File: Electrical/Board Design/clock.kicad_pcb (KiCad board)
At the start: 2 copper layers, 31 parts, among them CON1 AVR-ISP-6, IC1 ATTINY84A-SS, Q1 FET_N, Q2 FET_P, SW1 SPST, U1 MCP1624

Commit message: big catchup
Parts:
- added BT1: BATTERY, AA_battery_clip, F.Cu at (258.2, 216.9)
- added BT2: BATTERY, AA_battery_clip, F.Cu at (192.3, 216.9)
- added D1: DIODE, SIL-2, F.Cu at (200.8, 184.9)
- added D2: LED, SIL-2, F.Cu at (176.3, 181.9)
- added D3: LED, SIL-2, F.Cu at (226.7, 181.5)
- added SP1: SPEAKER, SIL-2, F.Cu at (200.8, 181.3)
- added X1: CRYSTAL 32.768kHz, CRYSTAL, F.Cu at (198.7, 201.6)
- S1: footprint bourns_encoder -> bourns_knob
- moved S1 227.0 mm to (249.3, 182.2)
- moved R12 220.7 mm to (252.3, 195.7)
- moved C6 220.7 mm to (256.1, 198.2)
- moved R11 220.7 mm to (256.1, 193.2)
- moved R9 219.5 mm to (248.0, 194.5)
- moved R10 217.2 mm to (243.2, 189.6)
- moved C5 216.3 mm to (243.2, 193.4)
- moved R3 171.2 mm to (142.6, 188.6), turned to 270 degrees
- moved R2 168.9 mm to (150.3, 182.2)
- moved Q1 168.9 mm to (146.2, 194.7)
- moved R1 168.9 mm to (146.2, 189.6)
- moved R4 167.1 mm to (149.9, 197.9)
- moved Q2 167.1 mm to (139.0, 188.5)
- moved SW1 165.4 mm to (136.9, 196.3)
- moved R15 158.4 mm to (225.4, 185.6)
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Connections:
- R12 pad 2: /INT 2 -> /INT 1
- R9 pad 1: /INT 1 -> /INT 2
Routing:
- net N-000002: track 0.00 -> 128.5 mm, vias 0 -> 4
- net VCC: track 0.00 -> 101.4 mm, vias 0 -> 5
- net GND: track 0.00 -> 67.4 mm, vias 0 -> 10
- net N-000004: track 0.00 -> 67.3 mm
- net /MODE SELECT POWER: track 0.00 -> 63.2 mm
- net /ALARM LIGHT: track 0.00 -> 57.7 mm, vias 0 -> 2
- net /INT 1: track 0.00 -> 56.6 mm
- net /MODE SELECT: track 0.00 -> 53.9 mm
- net /INT 2: track 0.00 -> 53.8 mm
- net /AM PM LIGHT: track 0.00 -> 47.4 mm, vias 0 -> 2
- net /ALARM BUZZER: track 0.00 -> 28.2 mm, vias 0 -> 3
- net N-000009: track 0.00 -> 26.5 mm, vias 0 -> 2
- net N-0000018: track 0.00 -> 20.8 mm
- net N-0000015: track 0.00 -> 18.6 mm
- net N-0000022: track 0.00 -> 17.2 mm
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- added copper zone on B.Cu, net GND
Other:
- board outline added: 133.3 x 44.5 mm
- board text removed: "AMMETERS"

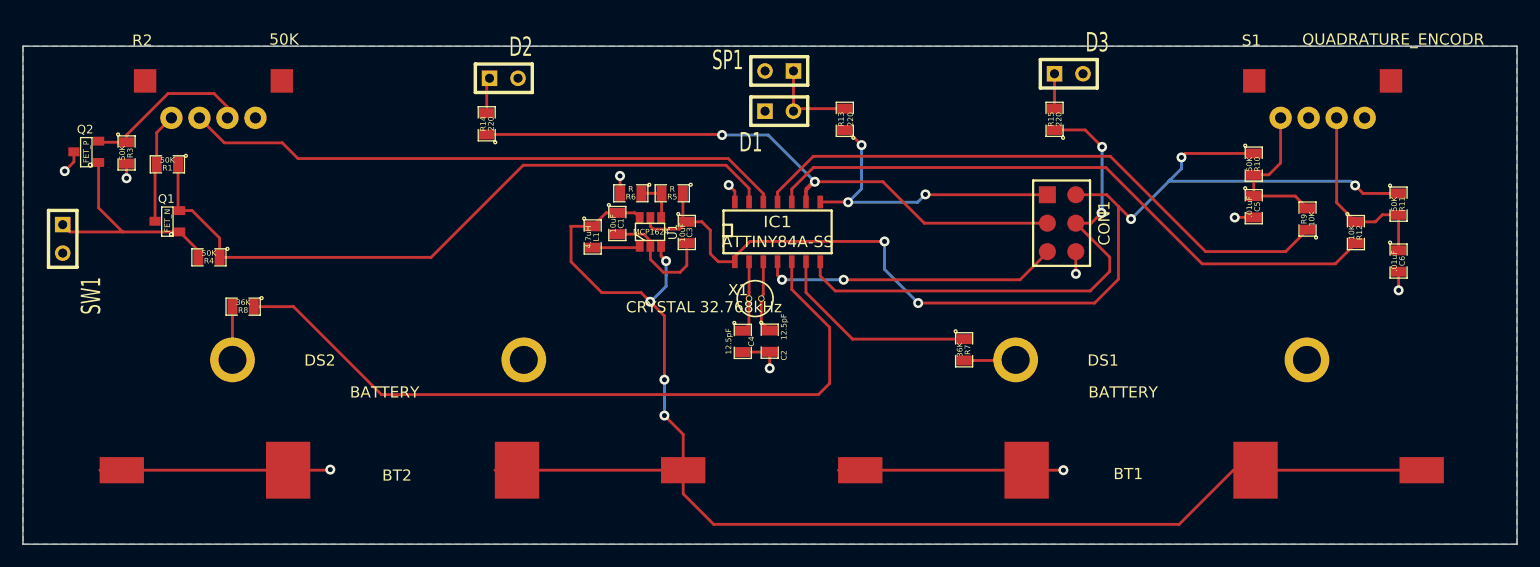
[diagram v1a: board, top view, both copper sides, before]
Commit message: board layout updates for battery stuff
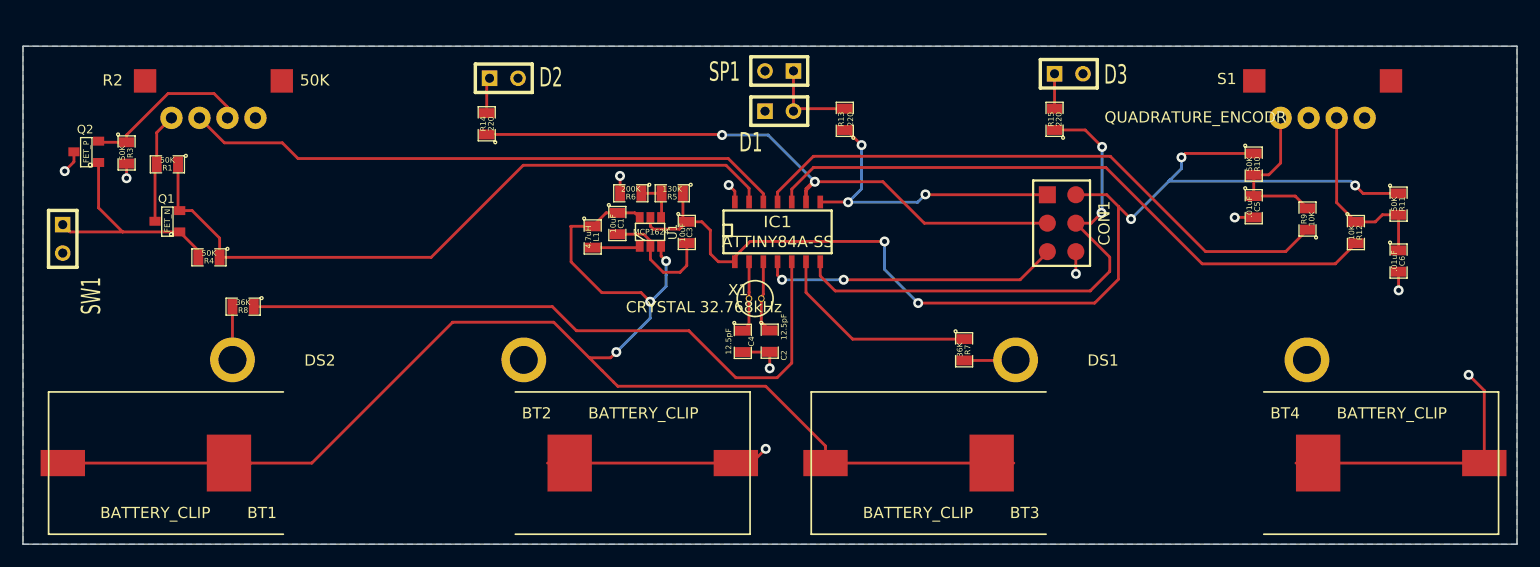
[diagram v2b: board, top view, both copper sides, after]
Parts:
- added BT3: BATTERY_CLIP, AA_battery_clip_single, F.Cu at (213.2, 216.3)
- added BT4: BATTERY_CLIP, AA_battery_clip_single, F.Cu at (255.5, 216.3)
- BT1, BT2: value BATTERY -> BATTERY_CLIP; footprint AA_battery_clip -> AA_battery_clip_single
- R5: value R -> 130K
- R6: value R -> 200K
- moved BT1 113.0 mm to (145.2, 216.3), turned to 270 degrees
- moved BT2 3.61 mm to (188.7, 216.3)
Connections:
- C1 pad 1: N-000002 (its old number) -> N-000006
- L1 pad 1: N-000002 (its old number) -> N-000006
- U1 pad 3: N-000002 (its old number) -> N-000006
- U1 pad 6: N-000002 (its old number) -> N-000006
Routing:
- net N-000006: track 0.00 -> 128.9 mm, vias 0 -> 3
- net N-000002 (its old number): track 128.5 -> 0.00 mm, vias 4 -> 0
- net N-000004: track 67.3 -> 60.2 mm
- net GND: track 67.4 -> 72.0 mm

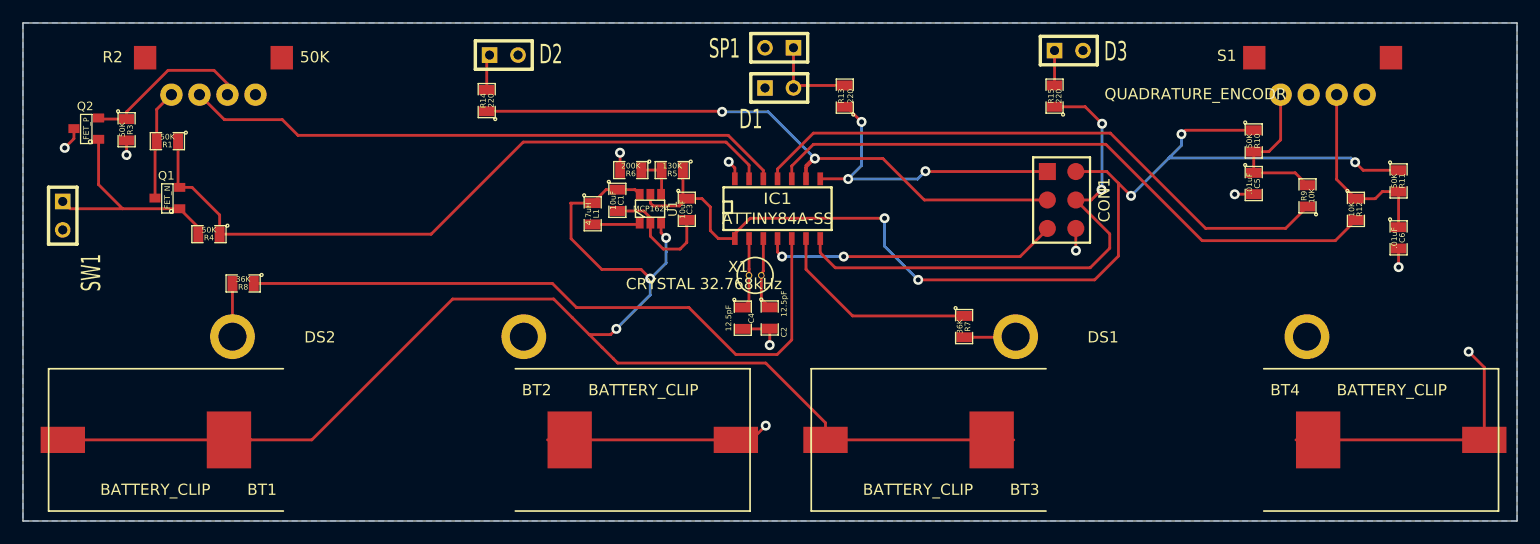
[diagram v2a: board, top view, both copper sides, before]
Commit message: updates to board layout
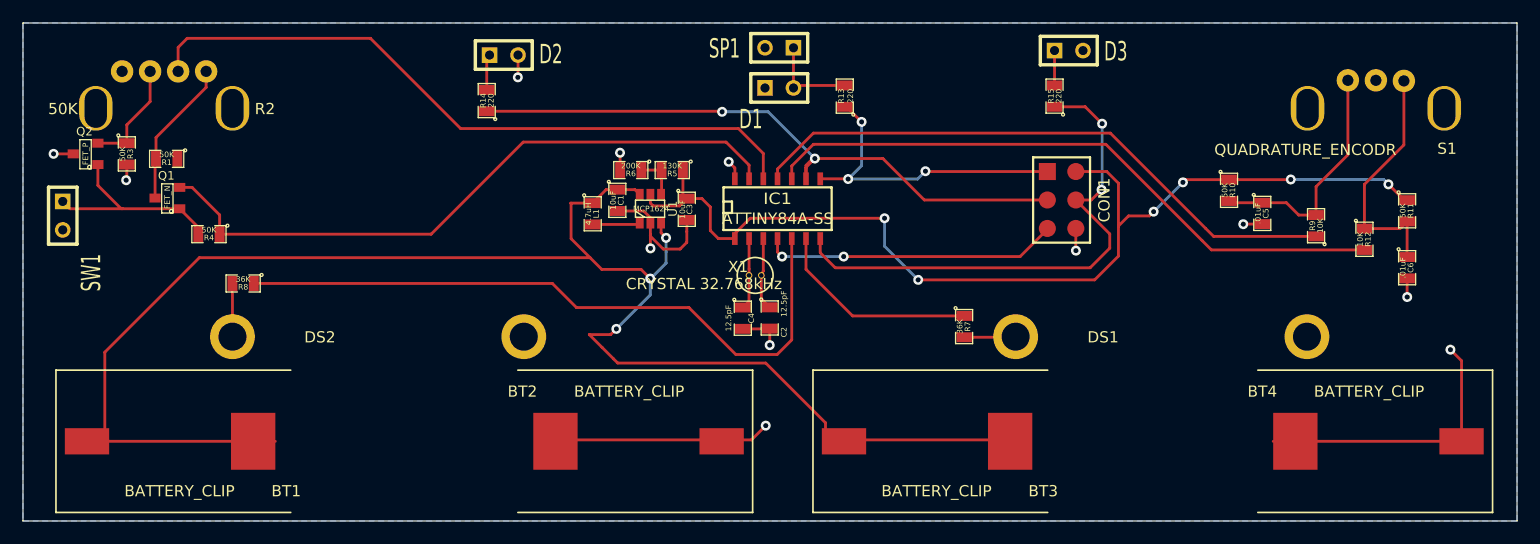
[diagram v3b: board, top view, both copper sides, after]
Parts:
- S1: footprint bourns_knob -> bourns_encoder
- moved S1 6.56 mm to (254.1, 186.7), turned to 180 degrees
- moved R2 6.31 mm to (145.9, 186.7), turned to 180 degrees
- moved R10 4.93 mm to (241.0, 194.0)
- moved C5 2.77 mm to (244.0, 196.1)
- moved C6 2.77 mm to (256.9, 200.9)
- moved R11 2.77 mm to (256.9, 195.8)
- moved R12 2.77 mm to (253.1, 198.4)
- moved R9 2.77 mm to (248.8, 197.2)
- moved Q2 2.25 mm to (138.9, 190.8)
- moved BT1 2.16 mm to (147.3, 216.4)
- moved R3 2.15 mm to (142.6, 190.8)
- moved BT4 2.04 mm to (253.5, 216.4)
- moved BT3 1.66 mm to (214.9, 216.4)
- moved R1 1.58 mm to (146.2, 191.2)
- moved BT2 1.28 mm to (187.5, 216.4)
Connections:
- C5 pad 1: N-000005 (its old number) -> N-0000021
- C6 pad 1: N-0000020 (its old number) -> N-000006
- R10 pad 2: N-000005 (its old number) -> N-0000021
- R11 pad 2: N-0000020 (its old number) -> N-000006
- R12 pad 1: N-0000020 (its old number) -> N-000006
- R9 pad 2: N-000005 (its old number) -> N-0000021
- S1 pad 1: N-000005 (its old number) -> N-000006
- S1 pad 3: N-0000020 (its old number) -> N-0000021
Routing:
- net N-000006: track 0.00 -> 21.9 mm
- net N-0000021: track 0.00 -> 21.5 mm
- net N-000007: track 128.9 -> 146.8 mm
- net N-0000020 (its old number): track 17.2 -> 0.00 mm
- net N-000005 (its old number): track 14.0 -> 0.00 mm
- net VCC: track 101.4 -> 92.9 mm, vias 5 -> 6
- net /MODE SELECT: track 53.9 -> 61.2 mm
- net N-0000017: track 15.2 -> 9.86 mm
- net /MODE SELECT POWER: track 63.2 -> 59.0 mm
- net N-0000016: track 9.83 -> 13.2 mm
- net GND: track 72.0 -> 75.2 mm, vias 10 -> 12
- net N-000003: track 20.8 -> 18.5 mm

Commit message: updated board layout
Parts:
- moved CON1 34.9 mm to (260.6, 200.1)
- moved C6 30.7 mm to (226.2, 198.9), turned to 0 degrees
- moved R12 29.0 mm to (224.2, 195.5), turned to 180 degrees
- moved R11 28.6 mm to (228.3, 195.4), turned to 180 degrees
- moved R9 25.2 mm to (224.1, 192.1), turned to 0 degrees
- moved C5 19.2 mm to (226.3, 188.6), turned to 0 degrees
- moved R1 17.8 mm to (164.0, 191.9)
- moved Q1 17.5 mm to (163.8, 195.0)
- moved Q2 15.6 mm to (153.8, 195.5)
- moved R3 15.4 mm to (157.3, 195.5)
- moved R4 13.9 mm to (163.9, 198.0)
- moved R10 12.9 mm to (228.3, 192.1), turned to 180 degrees
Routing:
- net /AM PM LIGHT: track 47.4 -> 100.0 mm
- net /ALARM BUZZER: track 28.2 -> 70.2 mm, vias 3 -> 2
- net /ALARM LIGHT: track 57.7 -> 93.9 mm
- net N-000008: track 26.5 -> 62.0 mm
- net /INT 1: track 57.0 -> 25.6 mm
- net VCC: track 92.9 -> 122.3 mm, vias 6 -> 4
- net /INT 2: track 54.1 -> 28.5 mm
- net N-000006: track 21.9 -> 44.3 mm
- net N-0000021: track 21.5 -> 41.0 mm
- net /MODE SELECT POWER: track 59.0 -> 45.1 mm
- net N-000003: track 18.5 -> 30.7 mm
- net N-0000016: track 13.2 -> 24.5 mm
- net N-0000017: track 9.86 -> 21.1 mm
- net GND: track 75.2 -> 75.8 mm
